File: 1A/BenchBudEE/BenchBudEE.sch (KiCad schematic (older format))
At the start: 0 parts

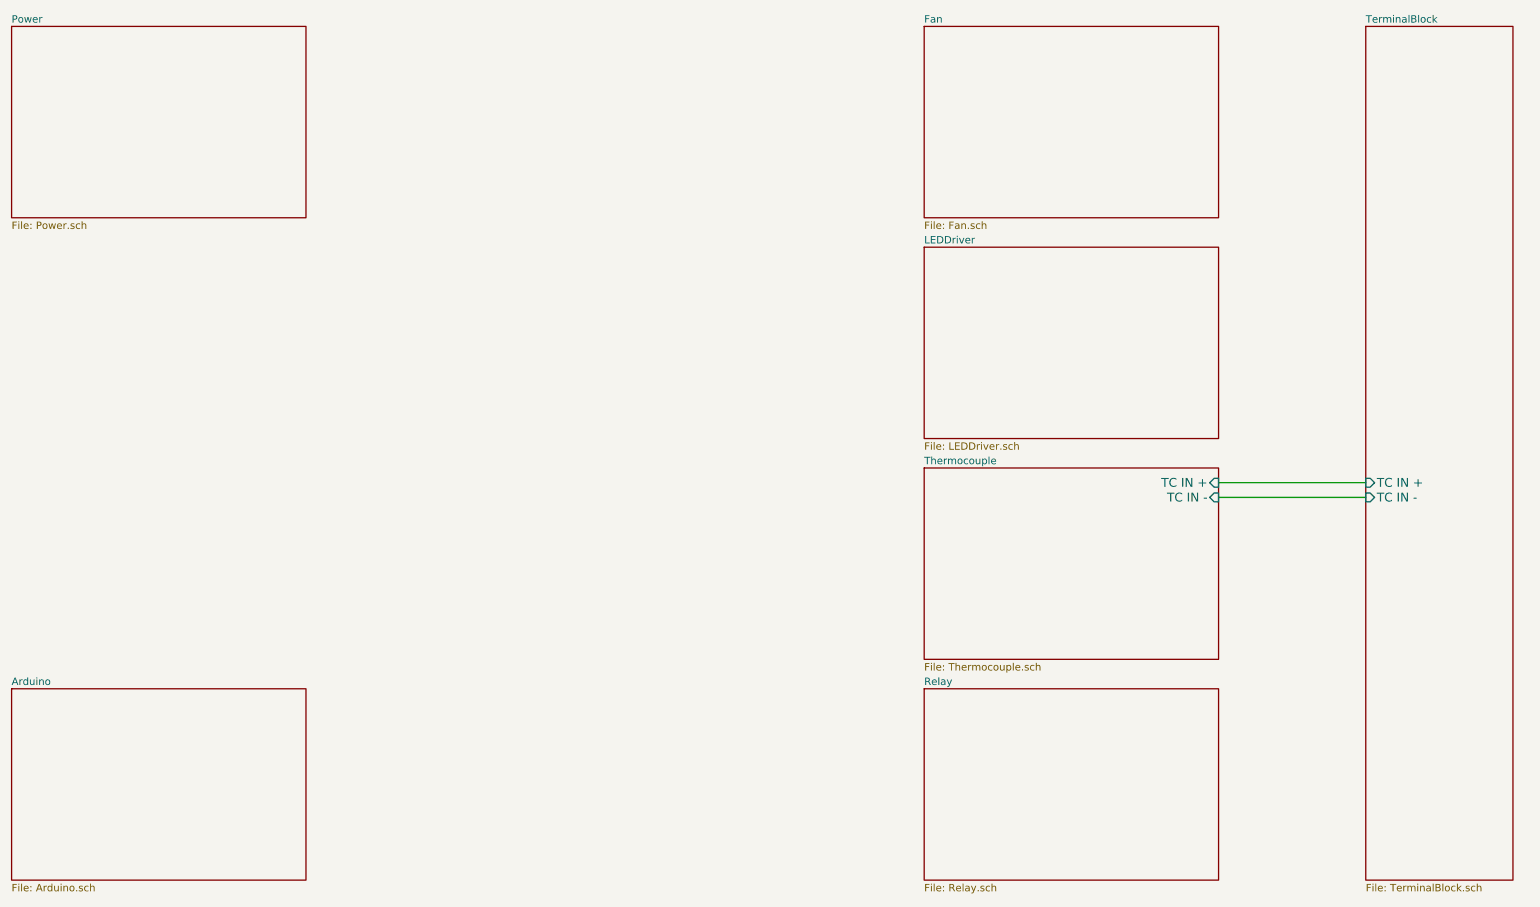
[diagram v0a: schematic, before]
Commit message: Define component inputs and outputs
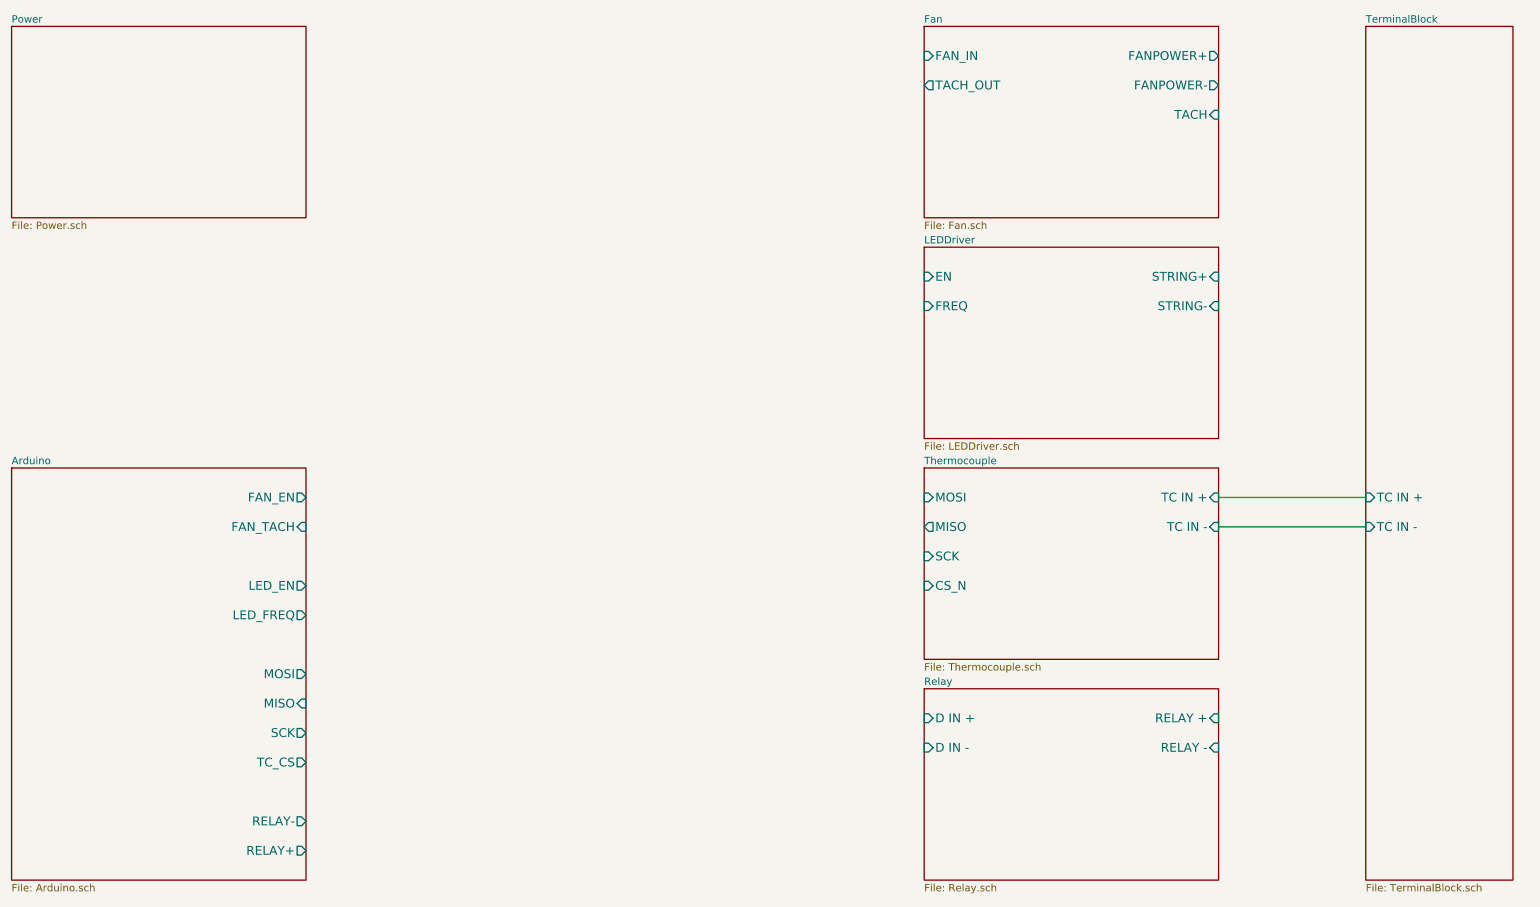
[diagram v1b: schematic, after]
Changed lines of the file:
@@
 $EndDescr
-$Sheet
-S 800  5200 2000 1300
-U 52EC0225
-F0 "Arduino" 50
-F1 "Arduino.sch" 50
-$EndSheet
-$Sheet
-S 7000 5200 2000 1300
-U 52EC0275
-F0 "Relay" 50
-F1 "Relay.sch" 50
-$EndSheet
 $Sheet
 S 800  700  2000 1300
@@
 $EndSheet
 $Sheet
-S 7000 2200 2000 1300
-U 52EC02BF
-F0 "LEDDriver" 50
-F1 "LEDDriver.sch" 50
+S 7000 700  2000 1300
+U 52EC02D2
+F0 "Fan" 50
+F1 "Fan.sch" 50
+F2 "FANPOWER+" O R 9000 900 60
+F3 "FANPOWER-" O R 9000 1100 60
+F4 "TACH" I R 9000 1300 60
+F5 "TACH_OUT" O L 7000 1100 60
+F6 "FAN_IN" I L 7000 900 60
+$EndSheet
+Wire Wire Line
+	9000 4100 10000 4100
+Wire Wire Line
+	9000 3900 10000 3900
+$Sheet
+S 7000 5200 2000 1300
+U 52EC0275
+F0 "Relay" 50
+F1 "Relay.sch" 50
+F2 "D IN +" I L 7000 5400 60
+F3 "D IN -" I L 7000 5600 60
+F4 "RELAY +" I R 9000 5400 60
+F5 "RELAY -" I R 9000 5600 60
+$EndSheet
+$Sheet
+S 800  3700 2000 2800
+U 52EC0225
+F0 "Arduino" 50
+F1 "Arduino.sch" 50
+F2 "RELAY+" O R 2800 6300 60
+F3 "RELAY-" O R 2800 6100 60
+F4 "MOSI" O R 2800 5100 60
+F5 "MISO" I R 2800 5300 60
+F6 "SCK" O R 2800 5500 60
+F7 "TC_CS" O R 2800 5700 60
+F8 "LED_EN" O R 2800 4500 60
+F9 "LED_FREQ" O R 2800 4700 60
+F10 "FAN_EN" O R 2800 3900 60
+F11 "FAN_TACH" I R 2800 4100 60
 $EndSheet
 $Sheet
@@
 F0 "TerminalBlock" 50
 F1 "TerminalBlock.sch" 50
-F2 "TC IN +" I L 10000 3800 60
-F3 "TC IN -" I L 10000 3900 60
-$EndSheet
-$Sheet
-S 7000 700  2000 1300
-U 52EC02D2
-F0 "Fan" 50
-F1 "Fan.sch" 50
+F2 "TC IN +" I L 10000 3900 60
+F3 "TC IN -" I L 10000 4100 60
 $EndSheet
 $Sheet
@@
 F0 "Thermocouple" 50
 F1 "Thermocouple.sch" 50
-F2 "TC IN -" I R 9000 3900 60
-F3 "TC IN +" I R 9000 3800 60
+F2 "TC IN -" I R 9000 4100 60
+F3 "TC IN +" I R 9000 3900 60
+F4 "MOSI" I L 7000 3900 60
+F5 "MISO" O L 7000 4100 60
+F6 "SCK" I L 7000 4300 60
+F7 "CS_N" I L 7000 4500 60
 $EndSheet
-Wire Wire Line
-	9000 3800 10000 3800
-Wire Wire Line
-	9000 3900 10000 3900
+$Sheet
+S 7000 2200 2000 1300
+U 52EC02BF
+F0 "LEDDriver" 50
+F1 "LEDDriver.sch" 50
+F2 "EN" I L 7000 2400 60
+F3 "FREQ" I L 7000 2600 60
+F4 "STRING+" I R 9000 2400 60
+F5 "STRING-" I R 9000 2600 60
+$EndSheet
 $EndSCHEMATC
